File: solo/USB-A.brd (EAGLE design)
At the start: 42.8 x 15 mm, 26 parts, among them U1 USB_TRACES

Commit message: use hatched footprints, remove bridge
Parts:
- removed SJ2: (no value), jumper:SJ
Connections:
- removed net N$23: N2.P1, SJ2.1
- net +3V3: now also N2.P1; no longer SJ2.2
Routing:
- net N$23: track 15.1 -> 0.00 mm, vias 2 -> 0
- net +3V3: track 79.2 -> 76.6 mm
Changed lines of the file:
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@@
 <attribute name="NAME" x="50.75" y="53.45" size="0.4064" layer="25"/>
 </element>
-<element name="U$2" library="efm-fido" library_urn="urn:adsk.eagle:library:4245354" package="DOME-BL-12MM" package3d_urn="urn:adsk.eagle:package:5648519/5" value="DOME_BUTTON12MM" x="64.4" y="54.15" smashed="yes"/>
-<element name="N2" library="efm-fido" library_urn="urn:adsk.eagle:library:4245354" package="MLPD3X3" package3d_urn="urn:adsk.eagle:package:5825738/3" value="AMS3956" x="74.1" y="57.45" smashed="yes" rot="R180">
+<element name="U$2" library="efm-fido" library_urn="urn:adsk.eagle:library:4245354" package="DOME-BL-12MM" package3d_urn="urn:adsk.eagle:package:5648519/7" value="DOME_BUTTON12MM" x="64.4" y="54.15" smashed="yes"/>
+<element name="N2" library="efm-fido" library_urn="urn:adsk.eagle:library:4245354" package="MLPD3X3" package3d_urn="urn:adsk.eagle:package:5825738/4" value="AMS3956" x="74.1" y="57.45" smashed="yes" rot="R180">
 <attribute name="NAME" x="74.5" y="59.35" size="0.6096" layer="25" rot="R270"/>
-<attribute name="VALUE" x="74.6" y="61.45" size="0.6096" layer="27" rot="R180"/>
-</element>
-<element name="SJ2" library="jumper" library_urn="urn:adsk.eagle:library:252" package="SJ" package3d_urn="urn:adsk.eagle:package:15471/1" value="" x="73.15" y="49.95" smashed="yes" rot="R180">
-<attribute name="NAME" x="74.201" y="48.607" size="0.8128" layer="25" ratio="10" rot="R180"/>
-<attribute name="VALUE" x="72.7499" y="49.95" size="0.02" layer="27" rot="R180"/>
+<attribute name="VALUE" x="74.6" y="61.25" size="0.6096" layer="27" rot="R180"/>
 </element>
 <element name="COIL2" library="efm-fido" library_urn="urn:adsk.eagle:library:4245354" package="MOLEX_NFC_COIL1" package3d_urn="urn:adsk.eagle:package:7114966/5" value="MOLEX_NFC_COIL_1462360101" x="46" y="46.35" smashed="yes" rot="MR90">
 <attribute name="LINK" value="https://www.mouser.com/ProductDetail/538-146236-0101" x="46" y="46.35" size="1.778" layer="28" rot="MR90" display="off"/>
 <attribute name="MPN" value="1462360101" x="46" y="46.35" size="1.778" layer="28" rot="MR90" display="off"/>
-<attribute name="NAME" x="71.45" y="57.13" size="0.8128" layer="25" rot="MR90"/>
+<attribute name="NAME" x="74.85" y="52.33" size="0.8128" layer="25" rot="MR90"/>
 <attribute name="VALUE" x="68" y="56.78" size="0.8128" layer="27" rot="MR90" display="off"/>
 </element>
@@
 <via x="50.65" y="49.95" extent="1-16" drill="0.35"/>
 <wire x1="74.1" y1="59.99" x2="73.6" y2="59.99" width="0.1524" layer="1"/>
-<wire x1="73.6" y1="59.99" x2="72.6" y2="58.99" width="0.1524" layer="1"/>
-<wire x1="72.298" y1="58.99" x2="72.6" y2="58.99" width="0.1524" layer="1"/>
-<via x="72.298" y="58.99" extent="1-16" drill="0.35"/>
+<wire x1="73.6" y1="59.99" x2="72.503065625" y2="59.09250625" width="0.1524" layer="1"/>
+<wire x1="72.498" y1="59.09" x2="72.503065625" y2="59.09250625" width="0.1524" layer="1"/>
+<via x="72.498" y="59.09" extent="1-16" drill="0.35"/>
 </signal>
 <signal name="+5V">
@@
 <via x="51.8" y="57.5" extent="1-16" drill="0.35"/>
 <wire x1="51.8" y1="57.5" x2="52.65" y2="56.65" width="0.254" layer="16"/>
-<wire x1="52.65" y1="56.65" x2="52.65" y2="55.6" width="0.254" layer="16"/>
-<wire x1="52.65" y1="55.6" x2="52.65" y2="49.05" width="0.254" layer="16"/>
+<wire x1="52.65" y1="56.65" x2="52.65" y2="49.05" width="0.254" layer="16"/>
 <wire x1="51.8" y1="57.5" x2="52.6" y2="57.5" width="0.254" layer="1"/>
 <wire x1="52.6" y1="57.5" x2="52.85" y2="57.75" width="0.254" layer="1"/>
@@
 <wire x1="57.5" y1="49.9" x2="58.15" y2="50.55" width="0.254" layer="16"/>
 <contactref element="N2" pad="P2"/>
-<contactref element="SJ2" pad="2"/>
 <wire x1="58.55" y1="52.5" x2="58.6" y2="52.5" width="0.3048" layer="1"/>
 <wire x1="58.55" y1="52.5" x2="58.025" y2="51.975" width="0.3048" layer="1"/>
@@
 <wire x1="54.0452" y1="48.5048" x2="54.0452" y2="48.49948125" width="0.3048" layer="1"/>
 <wire x1="54.0452" y1="48.49948125" x2="55.04468125" y2="47.5" width="0.3048" layer="1"/>
-<wire x1="55.04468125" y1="47.5" x2="71.25" y2="47.5" width="0.3048" layer="1"/>
-<wire x1="71.25" y1="47.5" x2="72.388" y2="48.638" width="0.3048" layer="1"/>
-<wire x1="72.388" y1="48.638" x2="72.388" y2="49.95" width="0.3048" layer="1"/>
+<wire x1="55.04468125" y1="47.5" x2="69.4" y2="47.5" width="0.3048" layer="1"/>
 <wire x1="74.7428" y1="56.9878" x2="74.7428" y2="58.3" width="0.3048" layer="1"/>
-<wire x1="71.33311875" y1="56.9878" x2="69.5122" y2="55.16688125" width="0.3048" layer="1"/>
-<wire x1="69.5122" y1="55.16688125" x2="69.5122" y2="52.93311875" width="0.3048" layer="1"/>
 <wire x1="74.7428" y1="56.9878" x2="71.33311875" y2="56.9878" width="0.3048" layer="1"/>
-<wire x1="72.388" y1="50.05731875" x2="72.388" y2="49.95" width="0.3048" layer="1"/>
-<wire x1="69.5122" y1="52.93311875" x2="72.388" y2="50.05731875" width="0.3048" layer="1"/>
+<wire x1="69.6122" y1="52.83311875" x2="70.672659375" y2="51.772659375" width="0.3048" layer="1"/>
 <wire x1="74.1" y1="58.49" x2="74.5528" y2="58.49" width="0.3048" layer="1"/>
 <wire x1="74.5528" y1="58.49" x2="74.7428" y2="58.3" width="0.3048" layer="1"/>
+<contactref element="N2" pad="P1"/>
+<wire x1="71.33311875" y1="56.9878" x2="69.6122" y2="55.26688125" width="0.3048" layer="1"/>
+<wire x1="69.6122" y1="55.26688125" x2="69.6122" y2="52.83311875" width="0.3048" layer="1"/>
+<wire x1="69.4" y1="47.5" x2="70.672659375" y2="48.772659375" width="0.3048" layer="1"/>
+<wire x1="70.672659375" y1="48.772659375" x2="70.672659375" y2="51.772659375" width="0.3048" layer="1"/>
+<wire x1="74.1" y1="58.49" x2="74.1" y2="57.99" width="0" layer="19" extent="1-1"/>
 </signal>
 <signal name="N$15">
@@
 <wire x1="58.3774" y1="60.4774" x2="55.15" y2="57.25" width="0.1524" layer="1"/>
 </signal>
-<signal name="N$23">
-<contactref element="SJ2" pad="1"/>
-<contactref element="N2" pad="P1"/>
-<wire x1="73.912" y1="49.95" x2="73.912" y2="51.213225" width="0.4064" layer="1"/>
-<wire x1="73.912" y1="51.213225" x2="73.9243875" y2="51.2256125" width="0.4064" layer="1"/>
-<via x="73.9243875" y="51.2256125" extent="1-16" drill="0.35"/>
-<wire x1="71.24364375" y1="51.2376" x2="69.5376" y2="52.94364375" width="0.254" layer="16"/>
-<wire x1="69.5376" y1="52.94364375" x2="69.5376" y2="55.15635625" width="0.254" layer="16"/>
-<wire x1="69.5376" y1="55.15635625" x2="70.190621875" y2="55.809378125" width="0.254" layer="16"/>
-<wire x1="73.9243875" y1="51.2256125" x2="73.9124" y2="51.2376" width="0.254" layer="16"/>
-<wire x1="73.9124" y1="51.2376" x2="71.24364375" y2="51.2376" width="0.254" layer="16"/>
-<wire x1="74.1" y1="57.99" x2="74.1" y2="57.69" width="0.3048" layer="1"/>
-<wire x1="74.1" y1="57.69" x2="73.91" y2="57.5" width="0.3048" layer="1"/>
-<wire x1="70.8" y1="57.5" x2="70.3" y2="57" width="0.3048" layer="1"/>
-<via x="70.3" y="57" extent="1-16" drill="0.35"/>
-<wire x1="70.3" y1="57" x2="70.3" y2="55.91875625" width="0.3048" layer="16"/>
-<wire x1="70.3" y1="55.91875625" x2="70.190621875" y2="55.809378125" width="0.3048" layer="16"/>
-<wire x1="73.91" y1="57.5" x2="70.8" y2="57.5" width="0.3048" layer="1"/>
-</signal>
 <signal name="AMS_CS">

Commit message: prep for nfc
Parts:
- removed COIL2: MOLEX_NFC_COIL_1462360101, efm-fido:MOLEX_NFC_COIL1
- added C2, C3, MID: .1u, efm-fido:C0402
- moved 3V1 7.52 mm to (52.5, 54.0)
- moved C7 7.52 mm to (59.0, 66.6)
- moved L4 7.52 mm to (57.0, 65.0)
- moved SRX<-1 7.52 mm to (63.6, 56.1)
- moved SWCLK1 7.52 mm to (57.5, 54.0)
- moved Z2 7.52 mm to (54.6, 59.2)
- moved L2 7.52 mm to (68.9, 60.9)
- moved C12 7.52 mm to (60.0, 56.5)
- moved D+1 7.52 mm to (55.8, 57.5)
- moved D-1 7.52 mm to (54.3, 61.6)
- moved U$2 7.52 mm to (68.5, 60.5)
- moved +5V1 7.52 mm to (55.2, 65.1)
- moved C10 7.52 mm to (54.8, 61.8)
- moved C8 7.52 mm to (59.0, 65.2)
- moved C9 7.52 mm to (54.8, 62.7)
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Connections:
- net N$25: now also C2.1, MID.2; no longer COIL2.P$1
- net N$26: now also C3.2, MID.1; no longer COIL2.P$2
- net PE: now also C2.2, C3.1
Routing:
- net PE: track 16.6 -> 99.9 mm, vias 18 -> 19
- net N$25: track 1.51 -> 2.89 mm
- net +3V3: track 76.6 -> 75.5 mm
- net N$26: track 3.28 -> 2.67 mm
- added copper zone on layer 16, net N$25
- added copper zone on layer 16, net N$26
- removed copper zone on layer 16, net PE
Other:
- board text added: "v1.4"
- board text removed: "v1.3"

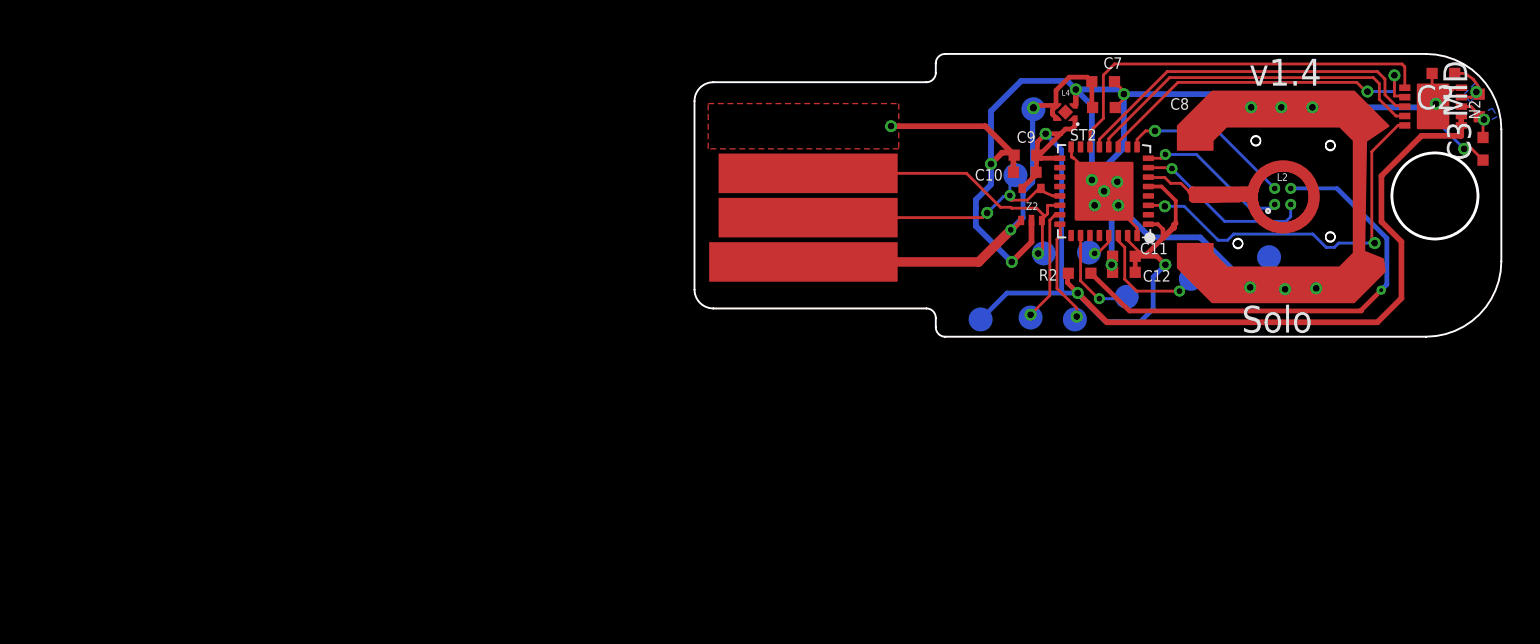
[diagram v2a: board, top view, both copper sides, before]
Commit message: NFC designs
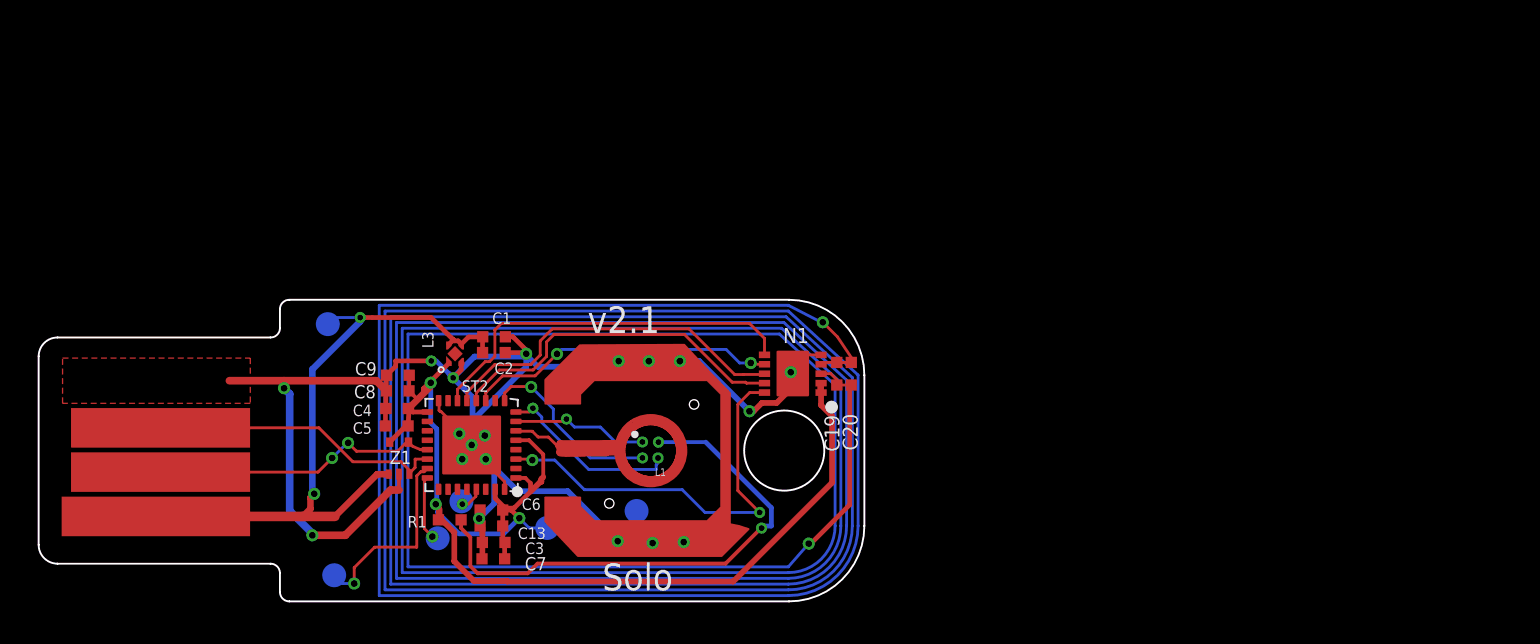
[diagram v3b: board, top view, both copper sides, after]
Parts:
- removed C10, C12: 4.7u, efm-fido:C0402
- removed C11, MID: .1u, efm-fido:C0402
- removed D+1, D-1, SRX<-1, SWO1: TEST_POINT, efm-fido:B1,27
- removed L2: EAST1616RGBA3-LED-RGBCL-505S-X-SD-T, efm-fido:CL-505S-X-SD-T
- removed L4: NCP114AMX330TCG, efm-fido:REG_NCP114AMX330TCG
- removed N2: AMS3956, efm-fido:MLPD3X3
- removed R2: 175, efm-fido:R0402
- removed U$2: DOME_BUTTON12MM, efm-fido:DOME-BL-12MM
- removed Z2: BZA900A-ESD-ZENERS, efm-fido:BZA900A
- added C1, C4, C6: .1u, efm-fido:C0402
- added C13, C5: 4.7u, efm-fido:C0402
- added C19, C20: .5p, efm-fido:C0402
- added L1: RGB_LED_1X1CL-505S-X-SD-T, efm-fido:CL-505S-X-SD-T
- added L3: NCP114AMX330TCG, efm-fido:REG_NCP114AMX330TCG
- added N1: AMS3956, efm-fido:MLPD3X3
- added R1: 175, efm-fido:R0402
- added U$1: DOME_BUTTON12MM, efm-fido:DOME-BL-12MM
- added Z1: BZA900A-ESD-ZENERS, efm-fido:BZA900A
- C2, C3, C7, C9: value .1u -> 4.7u
- moved C3 56.5 mm to (26.6, 42.1), turned to 180 degrees
- moved C2 52.5 mm to (26.6, 52.2), turned to 0 degrees
- moved C7 41.1 mm to (26.6, 41.2), turned to 180 degrees
- moved C8 40.4 mm to (21.5, 50.2), turned to 180 degrees
- moved SWDIO1 39.4 mm to (18.2, 40.4)
- moved +5V1 39.1 mm to (17.8, 53.7)
- moved U1 36.9 mm to (9.60, 47.0)
- moved GND1 36.1 mm to (34.2, 43.8)
- moved ST2 36.1 mm to (25.4, 47.3)
- moved STX->1 35.8 mm to (24.9, 44.3)
- moved SWCLK1 35.7 mm to (23.6, 42.3)
- moved C9 35.3 mm to (21.5, 51.0)
- moved 3V1 25.5 mm to (29.5, 42.9)
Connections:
- removed net AMS_CS: N2.P6, ST2.14
- removed net N$18: L2.P$3, ST2.7
- removed net N$19: ST2.6, U$2.P$1
- removed net N$25: C2.1, MID.2, N2.P4
- removed net N$26: C3.2, MID.1, N2.P3
- removed net SRX<-: SRX<-1.TP, ST2.30
- removed net SWO: ST2.26, SWO1.TP
- new net AMS_CS2: N1.P6, ST2.14
- new net N$1: L1.P$4, R1.1
- new net N$10: L1.P$3, ST2.8
- new net N$13: L1.P$2, ST2.9
- new net N$14: L1.P$1, ST2.7
- net +3V3: now also C13.1, C3.1, C4.1, C5.1, C6.1, C7.1, C8.1, L3.1, N1.P1, N1.P2, R1.2, Z1.P$5; no longer C10.1, C11.1, C12.1, L4.1, N2.P1, N2.P2, R2.2, Z2.P$5
- net +5V: now also C1.1, C2.1, L3.3, L3.4, Z1.P$1; no longer C7.1, C8.1, L4.3, L4.4, Z2.P$1
- net AMS_IRQ: now also N1.P10; no longer N2.P10
- net D+: now also Z1.P$3; no longer D+1.TP, Z2.P$3
- net D-: now also Z1.P$4; no longer D-1.TP, Z2.P$4
- net MISO: now also N1.P9; no longer N2.P9
- net MOSI: now also N1.P8; no longer N2.P8
- net N$15: now also ST2.6, U$1.P$1; no longer L2.P$4, R2.1
- net N$16: now also C19.2, C20.2, N1.P4; no longer L2.P$2, ST2.8
- net N$17: now also C19.1, C20.1, N1.P3; no longer L2.P$1, ST2.9
- net PE: now also C1.2, C13.2, C3.2, C4.2, C5.2, C6.2, L3.2, N1.P$11, N1.P5, U$1.P$2, Z1.P$2; no longer C10.2, C11.2, C12.2, C3.1, L4.2, N2.P$11, N2.P5, U$2.P$2, Z2.P$2
- net SCLK: now also N1.P7; no longer N2.P7
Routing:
- net N$2: track 0.00 -> 420.2 mm
- net N$1: track 0.00 -> 28.5 mm, vias 0 -> 2
- net AMS_CS: track 21.5 -> 0.00 mm
- net N$15: track 25.9 -> 4.63 mm, vias 2 -> 0
- net AMS_CS2: track 0.00 -> 20.4 mm
- net N$13: track 0.00 -> 9.81 mm, vias 0 -> 2
- net N$10: track 0.00 -> 9.79 mm, vias 0 -> 2
- net N$18: track 9.48 -> 0.00 mm, vias 2 -> 0
- net N$14: track 0.00 -> 7.34 mm, vias 0 -> 2
- net SRX<-: track 6.58 -> 0.00 mm, vias 1 -> 0
- net +3V3: track 75.5 -> 69.9 mm
- net SWO: track 5.55 -> 0.00 mm, vias 1 -> 0
- net N$19: track 4.63 -> 0.00 mm
- net +5V: track 31.6 -> 36.1 mm, vias 3 -> 2
- net PE: track 99.9 -> 104.2 mm
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- removed copper zone on layer 16, net N$25
- removed copper zone on layer 16, net N$26
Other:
- board size 42.8 x 15 mm -> 43.8 x 16 mm
- board text added: "v2.1"
- board text removed: "v1.4"
